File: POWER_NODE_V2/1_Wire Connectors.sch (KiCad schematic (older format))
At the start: 6 parts

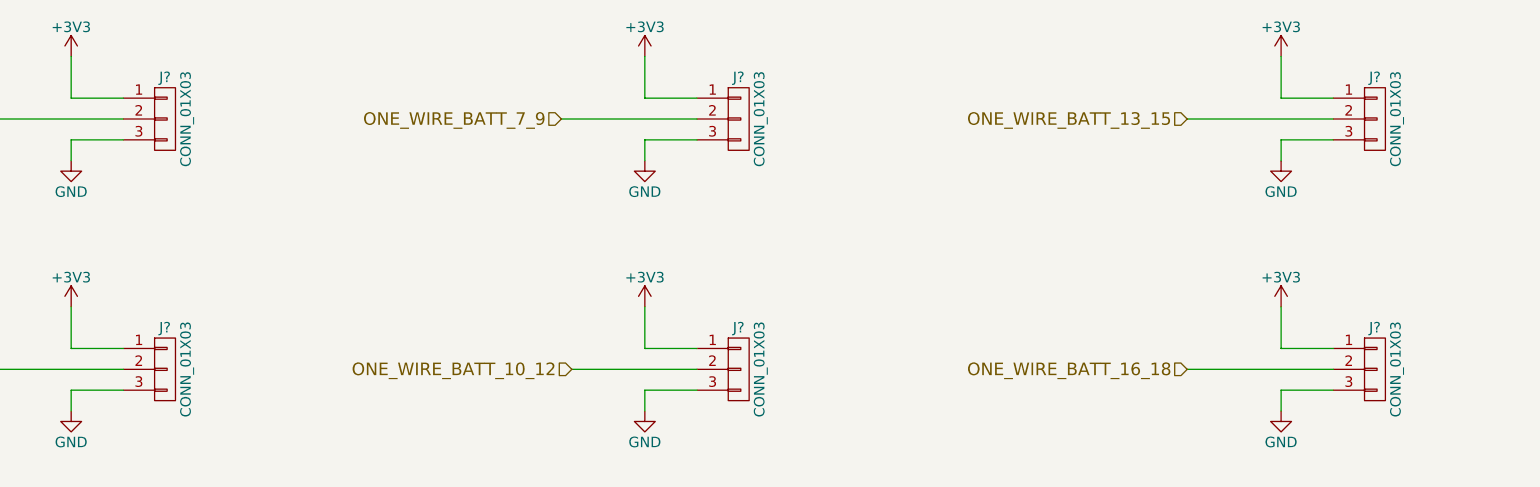
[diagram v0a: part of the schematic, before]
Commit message: made a lot of footprints, began PCB layout for power node v2
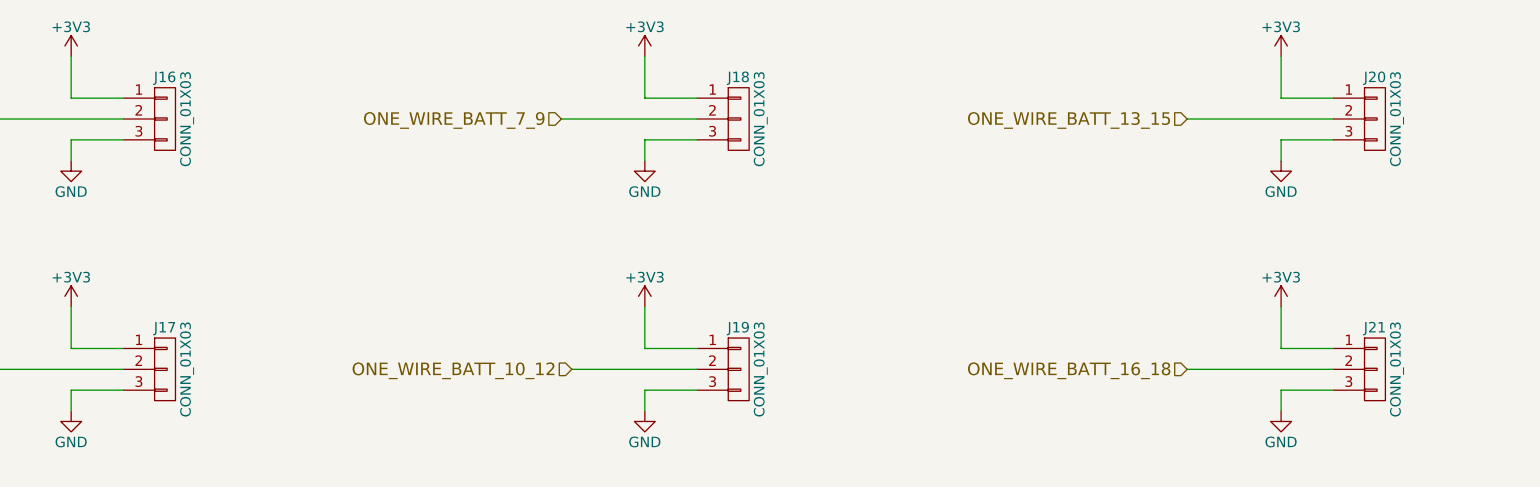
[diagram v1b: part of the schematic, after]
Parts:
- J16, J17, J18, J19, J20, J21: renamed from J?; footprint (none) -> Pin_Headers:Pin_Header_Straight_1x03_Pitch2.54mm
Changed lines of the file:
@@
 ONE_WIRE_BATT_16_18
 $Comp
-L CONN_01X03 J?
+L CONN_01X03 J16
 U 1 1 59524575
 P 3050 2400
-F 0 "J?" H 3050 2600 50  0000 C CNN
+F 0 "J16" H 3050 2600 50  0000 C CNN
 F 1 "CONN_01X03" V 3150 2400 50  0000 C CNN
-F 2 "" H 3050 2400 50  0001 C CNN
+F 2 "Pin_Headers:Pin_Header_Straight_1x03_Pitch2.54mm" H 3050 2400 50  0001 C CNN
 F 3 "" H 3050 2400 50  0001 C CNN
 	1    3050 2400
@@
 $EndComp
 $Comp
-L +3V3 #PWR?
+L +3V3 #PWR0133
 U 1 1 5952458C
 P 2600 2100
-F 0 "#PWR?" H 2600 1950 50  0001 C CNN
+F 0 "#PWR0133" H 2600 1950 50  0001 C CNN
 F 1 "+3V3" H 2600 2240 50  0000 C CNN
 F 2 "" H 2600 2100 50  0001 C CNN
@@
 $EndComp
 $Comp
-L GND #PWR?
+L GND #PWR0134
 U 1 1 595245A2
 P 2600 2600
-F 0 "#PWR?" H 2600 2350 50  0001 C CNN
+F 0 "#PWR0134" H 2600 2350 50  0001 C CNN
 F 1 "GND" H 2600 2450 50  0000 C CNN
 F 2 "" H 2600 2600 50  0001 C CNN
@@
 	2600 2500 2600 2600
 $Comp
-L CONN_01X03 J?
+L CONN_01X03 J17
 U 1 1 595245EE
 P 3050 3600
-F 0 "J?" H 3050 3800 50  0000 C CNN
+F 0 "J17" H 3050 3800 50  0000 C CNN
 F 1 "CONN_01X03" V 3150 3600 50  0000 C CNN
-F 2 "" H 3050 3600 50  0001 C CNN
+F 2 "Pin_Headers:Pin_Header_Straight_1x03_Pitch2.54mm" H 3050 3600 50  0001 C CNN
 F 3 "" H 3050 3600 50  0001 C CNN
 	1    3050 3600
@@
 $EndComp
 $Comp
-L +3V3 #PWR?
+L +3V3 #PWR0135
 U 1 1 595245F4
 P 2600 3300
-F 0 "#PWR?" H 2600 3150 50  0001 C CNN
+F 0 "#PWR0135" H 2600 3150 50  0001 C CNN
 F 1 "+3V3" H 2600 3440 50  0000 C CNN
 F 2 "" H 2600 3300 50  0001 C CNN
@@
 $EndComp
 $Comp
-L GND #PWR?
+L GND #PWR0136
 U 1 1 595245FA
 P 2600 3800
-F 0 "#PWR?" H 2600 3550 50  0001 C CNN
+F 0 "#PWR0136" H 2600 3550 50  0001 C CNN
 F 1 "GND" H 2600 3650 50  0000 C CNN
 F 2 "" H 2600 3800 50  0001 C CNN
@@
 	2600 3700 2600 3800
 $Comp
-L CONN_01X03 J?
+L CONN_01X03 J18
 U 1 1 595246C6
 P 5800 2400
-F 0 "J?" H 5800 2600 50  0000 C CNN
+F 0 "J18" H 5800 2600 50  0000 C CNN
 F 1 "CONN_01X03" V 5900 2400 50  0000 C CNN
-F 2 "" H 5800 2400 50  0001 C CNN
+F 2 "Pin_Headers:Pin_Header_Straight_1x03_Pitch2.54mm" H 5800 2400 50  0001 C CNN
 F 3 "" H 5800 2400 50  0001 C CNN
 	1    5800 2400
@@
 $EndComp
 $Comp
-L +3V3 #PWR?
+L +3V3 #PWR0137
 U 1 1 595246CC
 P 5350 2100
-F 0 "#PWR?" H 5350 1950 50  0001 C CNN
+F 0 "#PWR0137" H 5350 1950 50  0001 C CNN
 F 1 "+3V3" H 5350 2240 50  0000 C CNN
 F 2 "" H 5350 2100 50  0001 C CNN
@@
 $EndComp
 $Comp
-L GND #PWR?
+L GND #PWR0138
 U 1 1 595246D2
 P 5350 2600
-F 0 "#PWR?" H 5350 2350 50  0001 C CNN
+F 0 "#PWR0138" H 5350 2350 50  0001 C CNN
 F 1 "GND" H 5350 2450 50  0000 C CNN
 F 2 "" H 5350 2600 50  0001 C CNN
@@
 	5350 2500 5350 2600
 $Comp
-L CONN_01X03 J?
+L CONN_01X03 J19
 U 1 1 595246DC
 P 5800 3600
-F 0 "J?" H 5800 3800 50  0000 C CNN
+F 0 "J19" H 5800 3800 50  0000 C CNN
 F 1 "CONN_01X03" V 5900 3600 50  0000 C CNN
-F 2 "" H 5800 3600 50  0001 C CNN
+F 2 "Pin_Headers:Pin_Header_Straight_1x03_Pitch2.54mm" H 5800 3600 50  0001 C CNN
 F 3 "" H 5800 3600 50  0001 C CNN
 	1    5800 3600
@@
 $EndComp
 $Comp
-L +3V3 #PWR?
+L +3V3 #PWR0139
 U 1 1 595246E2
 P 5350 3300
-F 0 "#PWR?" H 5350 3150 50  0001 C CNN
+F 0 "#PWR0139" H 5350 3150 50  0001 C CNN
 F 1 "+3V3" H 5350 3440 50  0000 C CNN
 F 2 "" H 5350 3300 50  0001 C CNN
@@
 $EndComp
 $Comp
-L GND #PWR?
+L GND #PWR0140
 U 1 1 595246E8
 P 5350 3800
-F 0 "#PWR?" H 5350 3550 50  0001 C CNN
+F 0 "#PWR0140" H 5350 3550 50  0001 C CNN
 F 1 "GND" H 5350 3650 50  0000 C CNN
 F 2 "" H 5350 3800 50  0001 C CNN
@@
 	5350 3700 5350 3800
 $Comp
-L CONN_01X03 J?
+L CONN_01X03 J20
 U 1 1 59524738
 P 8850 2400
-F 0 "J?" H 8850 2600 50  0000 C CNN
+F 0 "J20" H 8850 2600 50  0000 C CNN
 F 1 "CONN_01X03" V 8950 2400 50  0000 C CNN
-F 2 "" H 8850 2400 50  0001 C CNN
+F 2 "Pin_Headers:Pin_Header_Straight_1x03_Pitch2.54mm" H 8850 2400 50  0001 C CNN
 F 3 "" H 8850 2400 50  0001 C CNN
 	1    8850 2400
@@
 $EndComp
 $Comp
-L +3V3 #PWR?
+L +3V3 #PWR0141
 U 1 1 5952473E
 P 8400 2100
-F 0 "#PWR?" H 8400 1950 50  0001 C CNN
+F 0 "#PWR0141" H 8400 1950 50  0001 C CNN
 F 1 "+3V3" H 8400 2240 50  0000 C CNN
 F 2 "" H 8400 2100 50  0001 C CNN
@@
 $EndComp
 $Comp
-L GND #PWR?
+L GND #PWR0142
 U 1 1 59524744
 P 8400 2600
-F 0 "#PWR?" H 8400 2350 50  0001 C CNN
+F 0 "#PWR0142" H 8400 2350 50  0001 C CNN
 F 1 "GND" H 8400 2450 50  0000 C CNN
 F 2 "" H 8400 2600 50  0001 C CNN
@@
 	8400 2500 8400 2600
 $Comp
-L CONN_01X03 J?
+L CONN_01X03 J21
 U 1 1 5952474E
 P 8850 3600
-F 0 "J?" H 8850 3800 50  0000 C CNN
+F 0 "J21" H 8850 3800 50  0000 C CNN
 F 1 "CONN_01X03" V 8950 3600 50  0000 C CNN
-F 2 "" H 8850 3600 50  0001 C CNN
+F 2 "Pin_Headers:Pin_Header_Straight_1x03_Pitch2.54mm" H 8850 3600 50  0001 C CNN
 F 3 "" H 8850 3600 50  0001 C CNN
 	1    8850 3600
@@
 $EndComp
 $Comp
-L +3V3 #PWR?
+L +3V3 #PWR0143
 U 1 1 59524754
 P 8400 3300
-F 0 "#PWR?" H 8400 3150 50  0001 C CNN
+F 0 "#PWR0143" H 8400 3150 50  0001 C CNN
 F 1 "+3V3" H 8400 3440 50  0000 C CNN
 F 2 "" H 8400 3300 50  0001 C CNN
@@
 $EndComp
 $Comp
-L GND #PWR?
+L GND #PWR0144
 U 1 1 5952475A
 P 8400 3800
-F 0 "#PWR?" H 8400 3550 50  0001 C CNN
+F 0 "#PWR0144" H 8400 3550 50  0001 C CNN
 F 1 "GND" H 8400 3650 50  0000 C CNN
 F 2 "" H 8400 3800 50  0001 C CNN

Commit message: Power Node v2 WIP
TODO: 3d models, double check everything, update connector P/N on
schematics, align boards and drill holes
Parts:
- J16, J17, J18, J19, J20, J21: footprint Pin_Headers:Pin_Header_Straight_1x03_Pitch2.54mm -> rLoop Footprints:3-641215-3_3Pin_Latching_Header
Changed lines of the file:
@@
 F 0 "J16" H 3050 2600 50  0000 C CNN
 F 1 "CONN_01X03" V 3150 2400 50  0000 C CNN
-F 2 "Pin_Headers:Pin_Header_Straight_1x03_Pitch2.54mm" H 3050 2400 50  0001 C CNN
+F 2 "rLoop Footprints:3-641215-3_3Pin_Latching_Header" H 3050 2400 50  0001 C CNN
 F 3 "" H 3050 2400 50  0001 C CNN
 	1    3050 2400
@@
 F 0 "J17" H 3050 3800 50  0000 C CNN
 F 1 "CONN_01X03" V 3150 3600 50  0000 C CNN
-F 2 "Pin_Headers:Pin_Header_Straight_1x03_Pitch2.54mm" H 3050 3600 50  0001 C CNN
+F 2 "rLoop Footprints:3-641215-3_3Pin_Latching_Header" H 3050 3600 50  0001 C CNN
 F 3 "" H 3050 3600 50  0001 C CNN
 	1    3050 3600
@@
 F 0 "J18" H 5800 2600 50  0000 C CNN
 F 1 "CONN_01X03" V 5900 2400 50  0000 C CNN
-F 2 "Pin_Headers:Pin_Header_Straight_1x03_Pitch2.54mm" H 5800 2400 50  0001 C CNN
+F 2 "rLoop Footprints:3-641215-3_3Pin_Latching_Header" H 5800 2400 50  0001 C CNN
 F 3 "" H 5800 2400 50  0001 C CNN
 	1    5800 2400
@@
 F 0 "J19" H 5800 3800 50  0000 C CNN
 F 1 "CONN_01X03" V 5900 3600 50  0000 C CNN
-F 2 "Pin_Headers:Pin_Header_Straight_1x03_Pitch2.54mm" H 5800 3600 50  0001 C CNN
+F 2 "rLoop Footprints:3-641215-3_3Pin_Latching_Header" H 5800 3600 50  0001 C CNN
 F 3 "" H 5800 3600 50  0001 C CNN
 	1    5800 3600
@@
 F 0 "J20" H 8850 2600 50  0000 C CNN
 F 1 "CONN_01X03" V 8950 2400 50  0000 C CNN
-F 2 "Pin_Headers:Pin_Header_Straight_1x03_Pitch2.54mm" H 8850 2400 50  0001 C CNN
+F 2 "rLoop Footprints:3-641215-3_3Pin_Latching_Header" H 8850 2400 50  0001 C CNN
 F 3 "" H 8850 2400 50  0001 C CNN
 	1    8850 2400
@@
 F 0 "J21" H 8850 3800 50  0000 C CNN
 F 1 "CONN_01X03" V 8950 3600 50  0000 C CNN
-F 2 "Pin_Headers:Pin_Header_Straight_1x03_Pitch2.54mm" H 8850 3600 50  0001 C CNN
+F 2 "rLoop Footprints:3-641215-3_3Pin_Latching_Header" H 8850 3600 50  0001 C CNN
 F 3 "" H 8850 3600 50  0001 C CNN
 	1    8850 3600

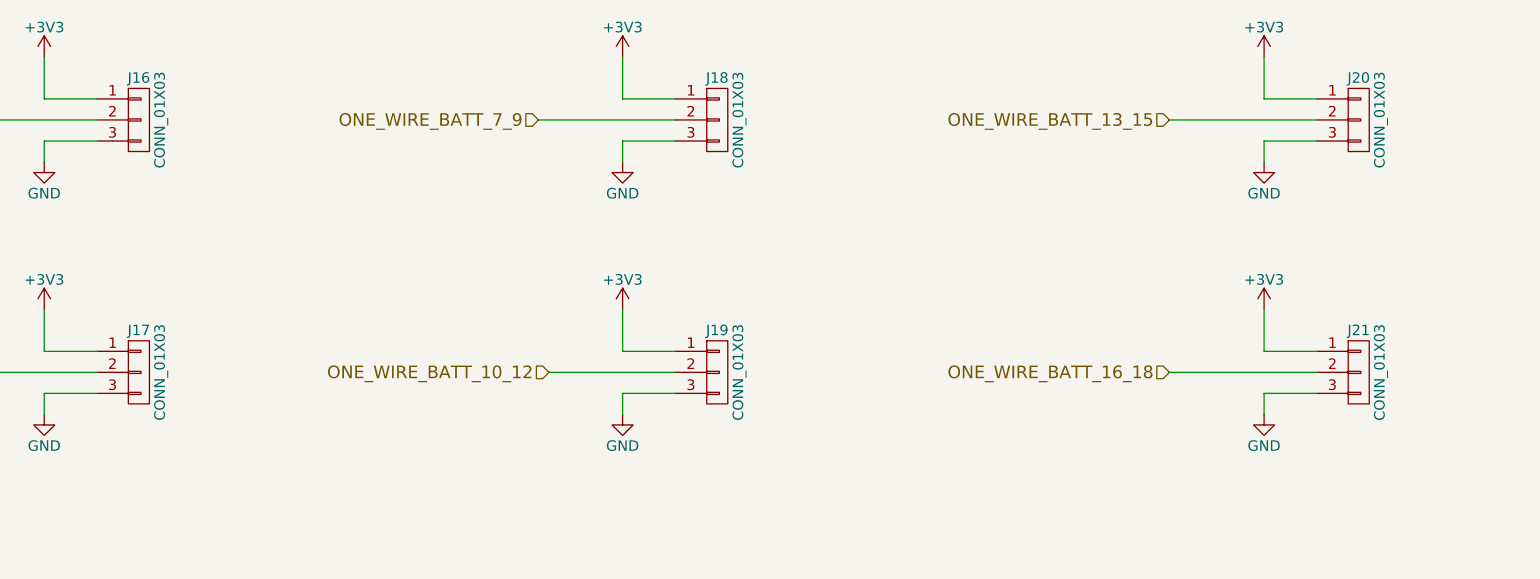
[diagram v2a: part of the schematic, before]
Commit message: 3d model work
TODO: change 2 pins to MTA156
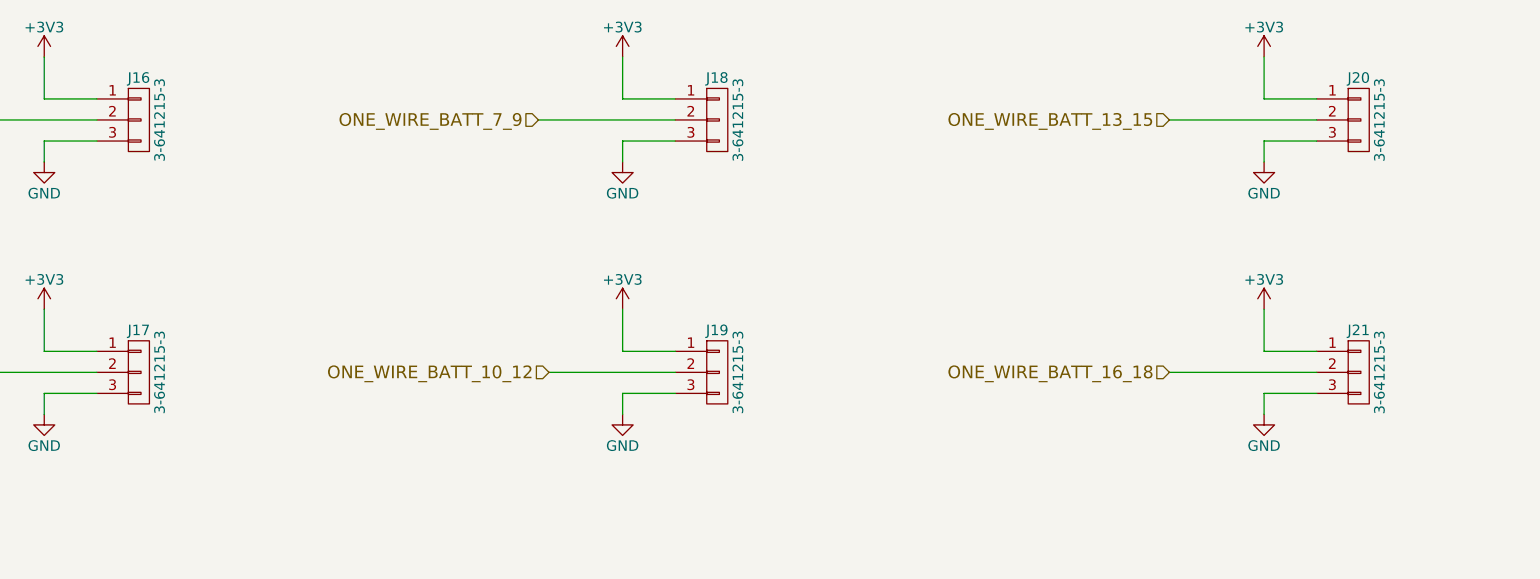
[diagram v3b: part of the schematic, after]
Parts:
- J16, J17, J18, J19, J20, J21: value CONN_01X03 -> 3-641215-3
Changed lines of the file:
@@
 P 3050 2400
 F 0 "J16" H 3050 2600 50  0000 C CNN
-F 1 "CONN_01X03" V 3150 2400 50  0000 C CNN
+F 1 "3-641215-3" V 3150 2400 50  0000 C CNN
 F 2 "rLoop Footprints:3-641215-3_3Pin_Latching_Header" H 3050 2400 50  0001 C CNN
 F 3 "" H 3050 2400 50  0001 C CNN
@@
 P 3050 3600
 F 0 "J17" H 3050 3800 50  0000 C CNN
-F 1 "CONN_01X03" V 3150 3600 50  0000 C CNN
+F 1 "3-641215-3" V 3150 3600 50  0000 C CNN
 F 2 "rLoop Footprints:3-641215-3_3Pin_Latching_Header" H 3050 3600 50  0001 C CNN
 F 3 "" H 3050 3600 50  0001 C CNN
@@
 P 5800 2400
 F 0 "J18" H 5800 2600 50  0000 C CNN
-F 1 "CONN_01X03" V 5900 2400 50  0000 C CNN
+F 1 "3-641215-3" V 5900 2400 50  0000 C CNN
 F 2 "rLoop Footprints:3-641215-3_3Pin_Latching_Header" H 5800 2400 50  0001 C CNN
 F 3 "" H 5800 2400 50  0001 C CNN
@@
 P 5800 3600
 F 0 "J19" H 5800 3800 50  0000 C CNN
-F 1 "CONN_01X03" V 5900 3600 50  0000 C CNN
+F 1 "3-641215-3" V 5900 3600 50  0000 C CNN
 F 2 "rLoop Footprints:3-641215-3_3Pin_Latching_Header" H 5800 3600 50  0001 C CNN
 F 3 "" H 5800 3600 50  0001 C CNN
@@
 P 8850 2400
 F 0 "J20" H 8850 2600 50  0000 C CNN
-F 1 "CONN_01X03" V 8950 2400 50  0000 C CNN
+F 1 "3-641215-3" V 8950 2400 50  0000 C CNN
 F 2 "rLoop Footprints:3-641215-3_3Pin_Latching_Header" H 8850 2400 50  0001 C CNN
 F 3 "" H 8850 2400 50  0001 C CNN
@@
 P 8850 3600
 F 0 "J21" H 8850 3800 50  0000 C CNN
-F 1 "CONN_01X03" V 8950 3600 50  0000 C CNN
+F 1 "3-641215-3" V 8950 3600 50  0000 C CNN
 F 2 "rLoop Footprints:3-641215-3_3Pin_Latching_Header" H 8850 3600 50  0001 C CNN
 F 3 "" H 8850 3600 50  0001 C CNN

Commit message: Lot's of progress
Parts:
- J16, J17, J18, J19, J20, J21: footprint rLoop Footprints:3-641215-3_3Pin_Latching_Header -> rLoop_Footprints:3-641215-3_3Pin_Latching_Header
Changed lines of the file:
@@
 F 0 "J16" H 3050 2600 50  0000 C CNN
 F 1 "3-641215-3" V 3150 2400 50  0000 C CNN
-F 2 "rLoop Footprints:3-641215-3_3Pin_Latching_Header" H 3050 2400 50  0001 C CNN
+F 2 "rLoop_Footprints:3-641215-3_3Pin_Latching_Header" H 3050 2400 50  0001 C CNN
 F 3 "" H 3050 2400 50  0001 C CNN
 	1    3050 2400
@@
 F 0 "J17" H 3050 3800 50  0000 C CNN
 F 1 "3-641215-3" V 3150 3600 50  0000 C CNN
-F 2 "rLoop Footprints:3-641215-3_3Pin_Latching_Header" H 3050 3600 50  0001 C CNN
+F 2 "rLoop_Footprints:3-641215-3_3Pin_Latching_Header" H 3050 3600 50  0001 C CNN
 F 3 "" H 3050 3600 50  0001 C CNN
 	1    3050 3600
@@
 F 0 "J18" H 5800 2600 50  0000 C CNN
 F 1 "3-641215-3" V 5900 2400 50  0000 C CNN
-F 2 "rLoop Footprints:3-641215-3_3Pin_Latching_Header" H 5800 2400 50  0001 C CNN
+F 2 "rLoop_Footprints:3-641215-3_3Pin_Latching_Header" H 5800 2400 50  0001 C CNN
 F 3 "" H 5800 2400 50  0001 C CNN
 	1    5800 2400
@@
 F 0 "J19" H 5800 3800 50  0000 C CNN
 F 1 "3-641215-3" V 5900 3600 50  0000 C CNN
-F 2 "rLoop Footprints:3-641215-3_3Pin_Latching_Header" H 5800 3600 50  0001 C CNN
+F 2 "rLoop_Footprints:3-641215-3_3Pin_Latching_Header" H 5800 3600 50  0001 C CNN
 F 3 "" H 5800 3600 50  0001 C CNN
 	1    5800 3600
@@
 F 0 "J20" H 8850 2600 50  0000 C CNN
 F 1 "3-641215-3" V 8950 2400 50  0000 C CNN
-F 2 "rLoop Footprints:3-641215-3_3Pin_Latching_Header" H 8850 2400 50  0001 C CNN
+F 2 "rLoop_Footprints:3-641215-3_3Pin_Latching_Header" H 8850 2400 50  0001 C CNN
 F 3 "" H 8850 2400 50  0001 C CNN
 	1    8850 2400
@@
 F 0 "J21" H 8850 3800 50  0000 C CNN
 F 1 "3-641215-3" V 8950 3600 50  0000 C CNN
-F 2 "rLoop Footprints:3-641215-3_3Pin_Latching_Header" H 8850 3600 50  0001 C CNN
+F 2 "rLoop_Footprints:3-641215-3_3Pin_Latching_Header" H 8850 3600 50  0001 C CNN
 F 3 "" H 8850 3600 50  0001 C CNN
 	1    8850 3600
